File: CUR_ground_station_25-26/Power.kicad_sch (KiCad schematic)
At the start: 32 parts, among them J1 Conn_01x02, J2 UJ20-C-H-G-SMT-P16-TR, Q2 NTR4003N, SW5 PTS815SJM250SMTRLFS, U2 BQ24232RGT, U3 NCP186AMX330TAG, U4 USBLC6-2SC6

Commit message: switched battery connector, put mounting holes in place
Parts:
- J1: footprint Connector_JST:JST_PH_B2B-PH-K_1x02_P2.00mm_Vertical -> Connector_JST:JST_PH_S2B-PH-K_1x02_P2.00mm_Horizontal
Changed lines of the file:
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@@
 			)
 		)
-		(property "Footprint" "Connector_JST:JST_PH_B2B-PH-K_1x02_P2.00mm_Vertical"
+		(property "Footprint" "Connector_JST:JST_PH_S2B-PH-K_1x02_P2.00mm_Horizontal"
 			(at 30.48 30.48 0)
 			(effects

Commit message: labing, adding gnd vias, other cleanup
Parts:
- J1: footprint Connector_JST:JST_PH_S2B-PH-K_1x02_P2.00mm_Horizontal -> Connector_Molex:Molex_PicoBlade_53048-0210_1x02_P1.25mm_Horizontal
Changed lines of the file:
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@@
 			)
 		)
-		(property "Footprint" "Connector_JST:JST_PH_S2B-PH-K_1x02_P2.00mm_Horizontal"
+		(property "Footprint" "Connector_Molex:Molex_PicoBlade_53048-0210_1x02_P1.25mm_Horizontal"
 			(at 30.48 30.48 0)
 			(effects

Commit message: Update gerbers after rotating battery connector
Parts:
- J1: value Conn_01x02 -> 0530480210; MPN (none) -> 0530480210
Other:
- note added: "battery in question"
- note removed: "TODO: choose battery so we know connector and polarity"
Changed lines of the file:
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@@
 		)
 	)
-	(text "TODO:\nchoose battery\nso we know connector\nand polarity"
-		(exclude_from_sim no)
-		(at 40.386 28.448 0)
-		(effects
-			(font
-				(size 1.27 1.27)
-			)
-			(justify left top)
-		)
-	)
 	(text "Battery"
 		(exclude_from_sim no)
@@
 		)
 	)
+	(text "battery in question"
+		(exclude_from_sim no)
+		(at 23.622 48.514 0)
+		(effects
+			(font
+				(size 1.27 1.27)
+			)
+			(href "https://www.amazon.com/MakerHawk-Rechargeable-Protection-Insulated-Development/dp/B0D3LP6F8G")
+		)
+	)
 	(junction
 		(at 144.78 60.96)
@@
 			)
 		)
-		(property "Value" "Conn_01x02"
+		(property "Value" "0530480210"
 			(at 30.48 26.67 0)
 			(effects
@@
 			)
 		)
-		(property "Datasheet" "~"
+		(property "Datasheet" "https://www.molex.com/pdm_docs/sd/530480210_sd.pdf"
 			(at 30.48 30.48 0)
 			(effects
@@
 			(at 30.48 30.48 0)
 			(effects
+				(font
+					(size 1.27 1.27)
+				)
+				(hide yes)
+			)
+		)
+		(property "MPN" "0530480210"
+			(at 30.48 30.48 0)
+			(effects

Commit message: Update LDO and battery charger footprints
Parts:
- U2: footprint Package_DFN_QFN:VQFN-16-1EP_3x3mm_P0.5mm_EP1.68x1.68mm_ThermalVias -> Package_DFN_QFN:VQFN-16-1EP_3x3mm_P0.5mm_EP1.68x1.68mm
- U3: footprint XDFN8_1P6X1P2_onsemi:XDFN8_1P6X1P2_onsemi -> Regulator_Linear_onsemi:NCP186_XDFN8_1.6x1.2mm_P0.4mm
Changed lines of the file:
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@@
 			)
 		)
-		(property "Footprint" "Package_DFN_QFN:VQFN-16-1EP_3x3mm_P0.5mm_EP1.68x1.68mm_ThermalVias"
+		(property "Footprint" "Package_DFN_QFN:VQFN-16-1EP_3x3mm_P0.5mm_EP1.68x1.68mm"
 			(at 129.54 100.965 0)
 			(effects
@@
 			)
 		)
-		(property "Footprint" "XDFN8_1P6X1P2_onsemi:XDFN8_1P6X1P2_onsemi"
+		(property "Footprint" "Regulator_Linear_onsemi:NCP186_XDFN8_1.6x1.2mm_P0.4mm"
 			(at 68.58 114.3 0)
 			(effects

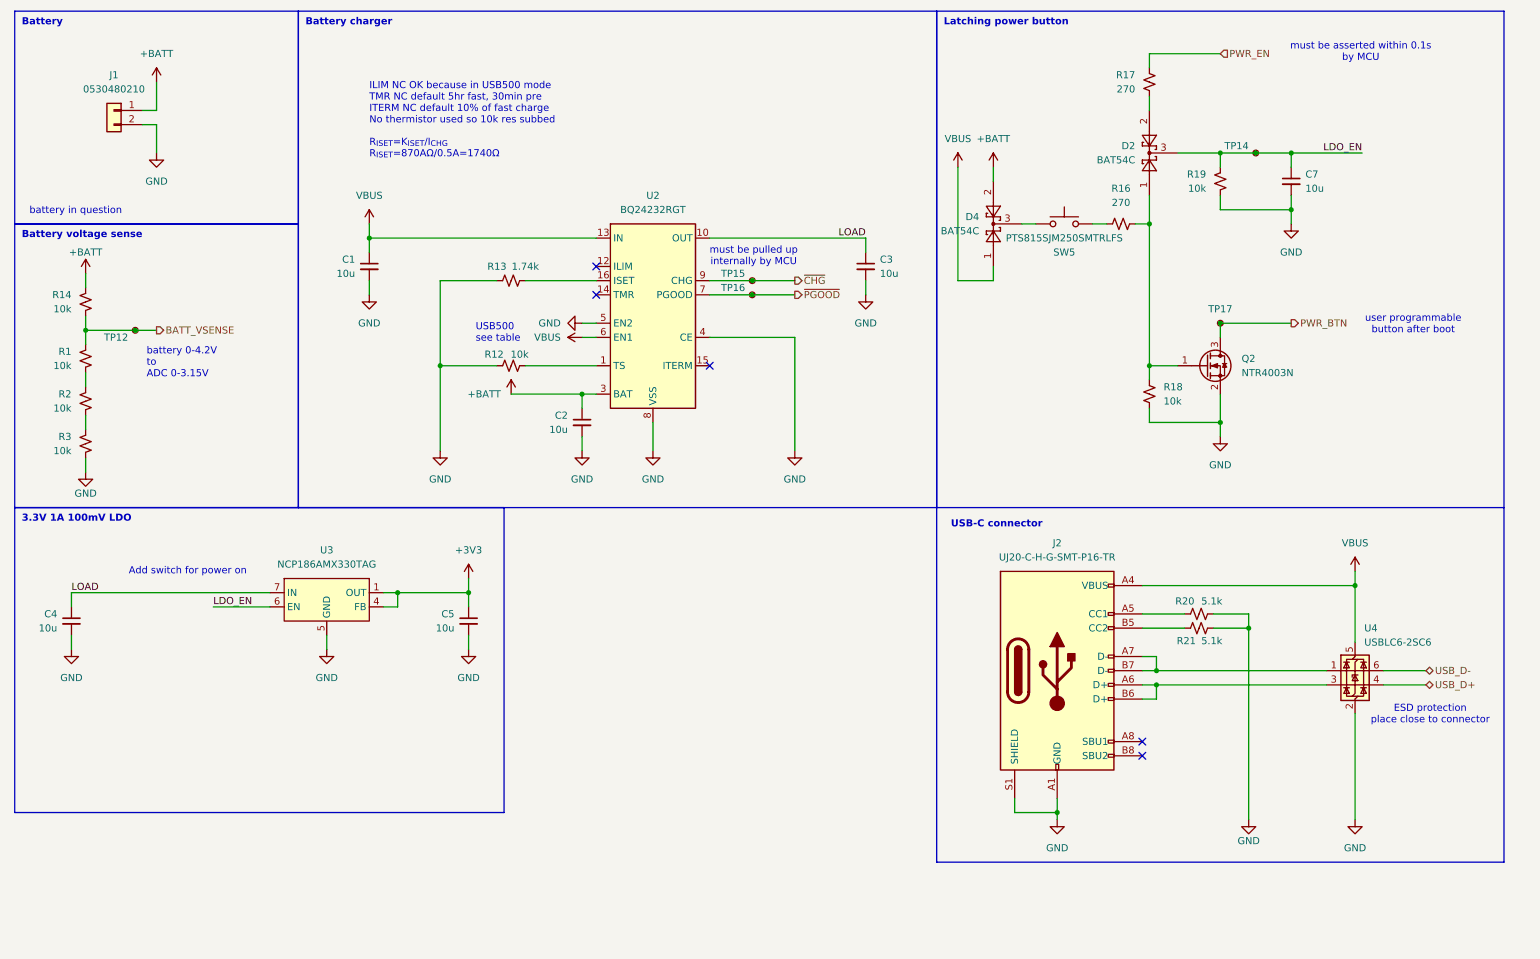
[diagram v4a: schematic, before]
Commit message: Find MPNs again
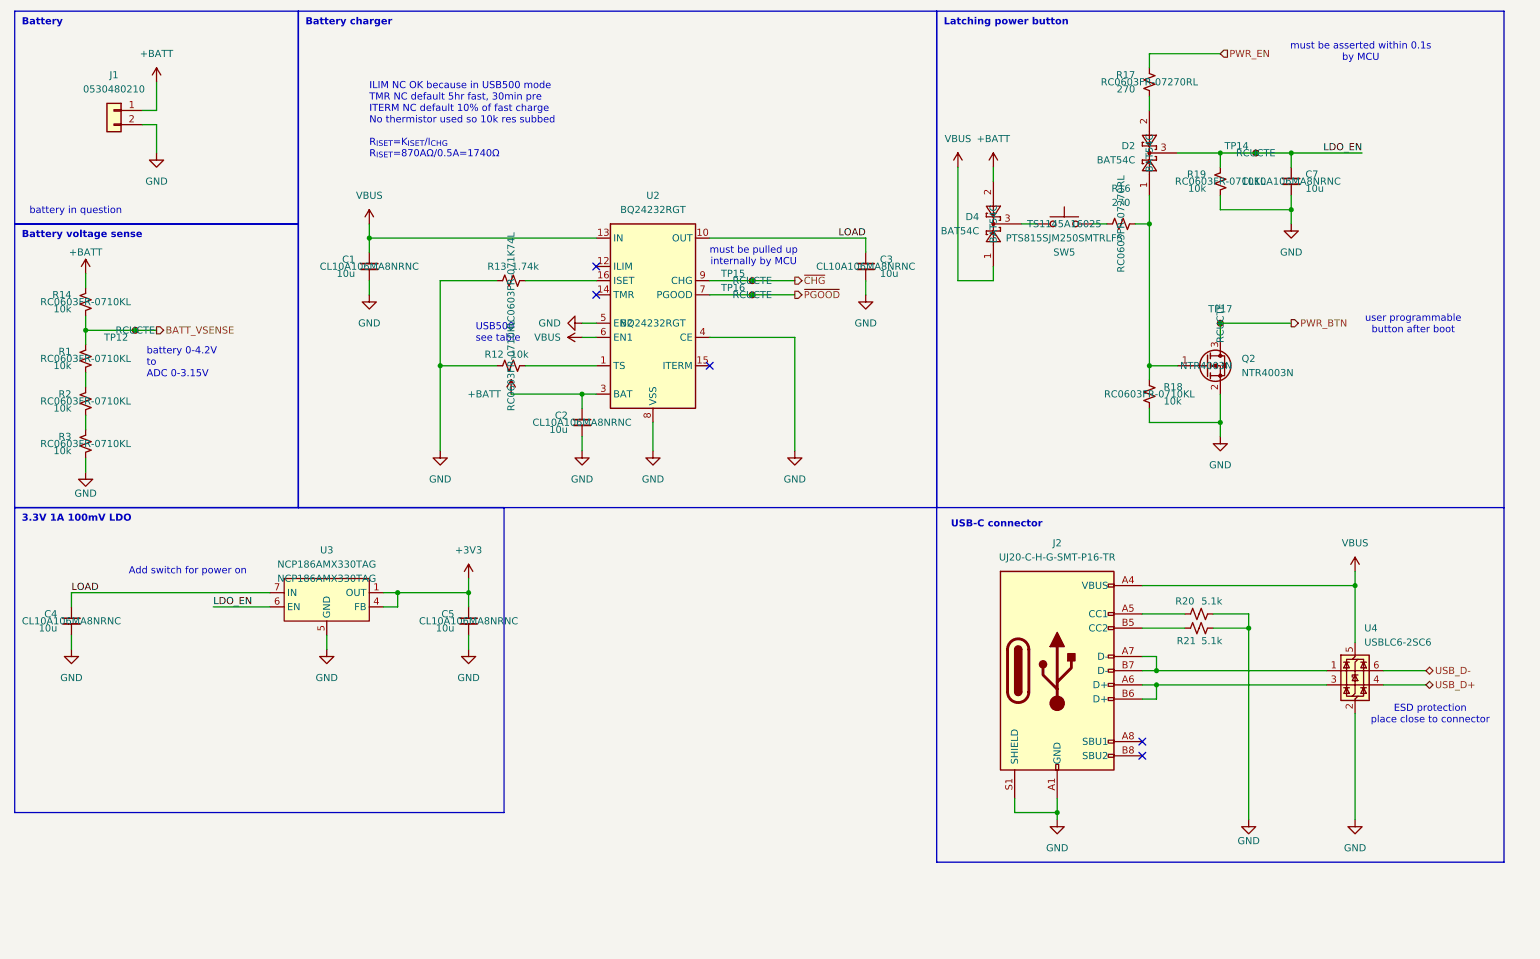
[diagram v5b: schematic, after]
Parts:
- C1, C2, C3, C4, C5, C7: MPN (none) -> CL10A106MA8NRNC
- D2, D4: MPN (none) -> BAT54C
- J1: MPN 0530480210 -> 1.25-2AW
- Q2: MPN (none) -> NTR4003N; now left out of the parts list
- R1, R12, R14, R18, R19, R2, R3: MPN (none) -> RC0603FR-0710KL
- R13: MPN (none) -> RC0603FR-071K74L
- R16, R17: MPN (none) -> RC0603FR-07270RL
- R20, R21: MPN RC0603FR-075K1L -> RC0603FR-075K1L
- SW5: MPN (none) -> TS1145A16025
- TP12, TP14, TP15, TP16, TP17: MPN (none) -> RCUCTE
- U2: MPN (none) -> BQ24232RGT
- U3: MPN (none) -> NCP186AMX330TAG
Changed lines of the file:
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@@
 			)
 		)
+		(property "MPN" "RCUCTE"
+			(at 144.78 60.96 0)
+			(effects
+				(font
+					(size 1.27 1.27)
+				)
+			)
+		)
 		(pin "1"
 		)
@@
 			)
 		)
+		(property "MPN" "CL10A106MA8NRNC"
+			(at 93.98 121.92 0)
+			(effects
+				(font
+					(size 1.27 1.27)
+				)
+			)
+		)
 		(pin "1"
 		)
@@
 			)
 		)
+		(property "MPN" "CL10A106MA8NRNC"
+			(at 241.3 43.18 0)
+			(effects
+				(font
+					(size 1.27 1.27)
+				)
+			)
+		)
 		(pin "2"
 		)
@@
 			)
 		)
+		(property "MPN" "BQ24232RGT"
+			(at 127 68.58 0)
+			(effects
+				(font
+					(size 1.27 1.27)
+				)
+			)
+		)
 		(pin "17"
 		)
@@
 			)
 		)
+		(property "MPN" "NCP186AMX330TAG"
+			(at 68.58 114.3 0)
+			(effects
+				(font
+					(size 1.27 1.27)
+				)
+			)
+		)
 		(pin "7"
 		)
@@
 			)
 		)
+		(property "MPN" "BAT54C"
+			(at 215.9 38.1 0)
+			(effects
+				(font
+					(size 1.27 1.27)
+				)
+			)
+		)
 		(pin "3"
 		)
@@
 			)
 		)
+		(property "MPN" "RC0603FR-0710KL"
+			(at 101.6 76.2 0)
+			(effects
+				(font
+					(size 1.27 1.27)
+				)
+			)
+		)
 		(pin "1"
 		)
@@
 			)
 		)
+		(property "MPN" "RC0603FR-0710KL"
+			(at 25.4 64.77 0)
+			(effects
+				(font
+					(size 1.27 1.27)
+				)
+			)
+		)
 		(pin "2"
 		)
@@
 			)
 		)
+		(property "MPN" "RCUCTE"
+			(at 34.29 69.85 0)
+			(effects
+				(font
+					(size 1.27 1.27)
+				)
+			)
+		)
 		(pin "1"
 		)
@@
 			)
 		)
+		(property "MPN" "RC0603FR-0710KL"
+			(at 25.4 82.55 0)
+			(effects
+				(font
+					(size 1.27 1.27)
+				)
+			)
+		)
 		(pin "2"
 		)
@@
 			)
 		)
-		(property "MPN" "RC0603FR-075K1L"
+		(property "MPN" " RC0603FR-075K1L"
 			(at 224.79 120.65 90)
 			(effects
@@
 			)
 		)
+		(property "MPN" "CL10A106MA8NRNC"
+			(at 165.1 58.42 0)
+			(effects
+				(font
+					(size 1.27 1.27)
+				)
+			)
+		)
 		(pin "2"
 		)
@@
 			)
 		)
+		(property "MPN" "RCUCTE"
+			(at 144.78 63.5 0)
+			(effects
+				(font
+					(size 1.27 1.27)
+				)
+			)
+		)
 		(pin "1"
 		)
@@
 			)
 		)
+		(property "MPN" "RCUCTE"
+			(at 234.95 38.1 0)
+			(effects
+				(font
+					(size 1.27 1.27)
+				)
+			)
+		)
 		(pin "1"
 		)
@@
 			)
 		)
+		(property "MPN" "RC0603FR-0710KL"
+			(at 228.6 43.18 0)
+			(effects
+				(font
+					(size 1.27 1.27)
+				)
+			)
+		)
 		(pin "2"
 		)
@@
 			)
 		)
+		(property "MPN" "CL10A106MA8NRNC"
+			(at 76.2 58.42 0)
+			(effects
+				(font
+					(size 1.27 1.27)
+				)
+			)
+		)
 		(pin "2"
 		)
@@
 			)
 		)
+		(property "MPN" "RC0603FR-071K74L"
+			(at 101.6 60.96 0)
+			(effects
+				(font
+					(size 1.27 1.27)
+				)
+			)
+		)
 		(pin "1"
 		)
@@
 			)
 		)
+		(property "MPN" "RC0603FR-0710KL"
+			(at 25.4 74.93 0)
+			(effects
+				(font
+					(size 1.27 1.27)
+				)
+			)
+		)
 		(pin "2"
 		)
@@
 			)
 		)
+		(property "MPN" "BAT54C"
+			(at 187.96 50.8 0)
+			(effects
+				(font
+					(size 1.27 1.27)
+				)
+			)
+		)
 		(pin "3"
 		)
@@
 			)
 		)
+		(property "MPN" "RC0603FR-07270RL"
+			(at 215.9 25.4 0)
+			(effects
+				(font
+					(size 1.27 1.27)
+				)
+			)
+		)
 		(pin "2"
 		)
@@
 			)
 		)
+		(property "MPN" "TS1145A16025"
+			(at 200.66 50.8 0)
+			(effects
+				(font
+					(size 1.27 1.27)
+				)
+			)
+		)
 		(pin "1"
 		)
@@
 			)
 		)
-		(property "MPN" "0530480210"
+		(property "MPN" "1.25-2AW"
 			(at 30.48 30.48 0)
 			(effects
@@
 			)
 		)
+		(property "MPN" "CL10A106MA8NRNC"
+			(at 22.86 121.92 0)
+			(effects
+				(font
+					(size 1.27 1.27)
+				)
+			)
+		)
 		(pin "1"
 		)
@@
 			)
 		)
-		(property "MPN" "RC0603FR-075K1L"
+		(property "MPN" " RC0603FR-075K1L"
 			(at 224.79 123.19 90)
 			(effects
@@
 			)
 		)
+		(property "MPN" "RCUCTE"
+			(at 228.6 68.58 0)
+			(effects
+				(font
+					(size 1.27 1.27)
+				)
+			)
+		)
 		(pin "1"
 		)
@@
 			)
 		)
+		(property "MPN" "CL10A106MA8NRNC"
+			(at 114.3 86.36 0)
+			(effects
+				(font
+					(size 1.27 1.27)
+				)
+			)
+		)
 		(pin "2"
 		)
@@
 		(unit 1)
 		(exclude_from_sim no)
-		(in_bom yes)
+		(in_bom no)
 		(on_board yes)
 		(dnp no)
@@
 			)
 		)
+		(property "MPN" "NTR4003N"
+			(at 226.06 76.2 0)
+			(effects
+				(font
+					(size 1.27 1.27)
+				)
+			)
+		)
 		(pin "3"
 		)
@@
 			)
 		)
+		(property "MPN" "RC0603FR-0710KL"
+			(at 25.4 90.17 0)
+			(effects
+				(font
+					(size 1.27 1.27)
+				)
+			)
+		)
 		(pin "2"
 		)
@@
 			)
 		)
+		(property "MPN" "RC0603FR-07270RL"
+			(at 210.82 50.8 0)
+			(effects
+				(font
+					(size 1.27 1.27)
+				)
+			)
+		)
 		(pin "1"
 		)
@@
 			)
 		)
+		(property "MPN" "RC0603FR-0710KL"
+			(at 215.9 81.28 0)
+			(effects
+				(font
+					(size 1.27 1.27)
+				)
+			)
+		)

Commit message: changes
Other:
- company: (none) -> Clarkson University Rocketry
- title: (none) -> Ground Station
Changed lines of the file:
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@@
 	(generator_version "9.0")
 	(paper "A4")
+	(title_block
+		(title "Ground Station")
+		(date "2026-04-29")
+		(company "Clarkson University Rocketry")
+	)
 	(rectangle
 		(start 177.8 12.7)
@@
 					(size 1.27 1.27)
 				)
+				(hide yes)
 			)
 		)
@@
 					(size 1.27 1.27)
 				)
+				(hide yes)
 			)
 		)
@@
 					(size 1.27 1.27)
 				)
+				(hide yes)
 			)
 		)
@@
 					(size 1.27 1.27)
 				)
+				(hide yes)
 			)
 		)
@@
 					(size 1.27 1.27)
 				)
+				(hide yes)
 			)
 		)
@@
 					(size 1.27 1.27)
 				)
+				(hide yes)
 			)
 		)
@@
 					(size 1.27 1.27)
 				)
+				(hide yes)
 			)
 		)
@@
 					(size 1.27 1.27)
 				)
+				(hide yes)
 			)
 		)
@@
 					(size 1.27 1.27)
 				)
+				(hide yes)
 			)
 		)
@@
 					(size 1.27 1.27)
 				)
+				(hide yes)
 			)
 		)
@@
 					(size 1.27 1.27)
 				)
+				(hide yes)
 			)
 		)
@@
 					(size 1.27 1.27)
 				)
+				(hide yes)
 			)
 		)
@@
 					(size 1.27 1.27)
 				)
+				(hide yes)
 			)
 		)
@@
 	)
 	(symbol
+		(lib_id "CUR_Logo:LOGO")
+		(at 279.4 173.99 0)
+		(unit 1)
+		(exclude_from_sim no)
+		(in_bom yes)
+		(on_board yes)
+		(dnp no)
+		(fields_autoplaced yes)
+		(property "Reference" "#G4"
+			(at 279.4 167.002 0)
+			(effects
+				(font
+					(size 1.27 1.27)
+				)
+				(hide yes)
+			)
+		)
+		(property "Value" "LOGO"
+			(at 279.4 180.978 0)
+			(effects
+				(font
+					(size 1.27 1.27)
+				)
+				(hide yes)
+			)
+		)
+		(property "Footprint" ""
+			(at 279.4 173.99 0)
+			(effects
+				(font
+					(size 1.27 1.27)
+				)
+				(hide yes)
+			)
+		)
+		(property "Datasheet" ""
+			(at 279.4 173.99 0)
+			(effects
+				(font
+					(size 1.27 1.27)
+				)
+				(hide yes)
+			)
+		)
+		(property "Description" ""
+			(at 279.4 173.99 0)
+			(effects
+				(font
+					(size 1.27 1.27)
+				)
+				(hide yes)
+			)
+		)
+		(instances
+			(project "CUR_ground_station_25-26"
+				(path "/b6f682bd-f29b-4650-adb4-b230be0368ad/81c93bb2-d3b4-4976-ae9e-2e07f946e0a4"
+					(reference "#G4")
+					(unit 1)
+				)
+			)
+		)
+	)
+	(symbol
 		(lib_id "Device:C_Small")
 		(at 76.2 58.42 0)
@@
 					(size 1.27 1.27)
 				)
+				(hide yes)
 			)
 		)
@@
 					(size 1.27 1.27)
 				)
+				(hide yes)
 			)
 		)
@@
 					(size 1.27 1.27)
 				)
+				(hide yes)
 			)
 		)
@@
 					(size 1.27 1.27)
 				)
+				(hide yes)
 			)
 		)
@@
 					(size 1.27 1.27)
 				)
+				(hide yes)
 			)
 		)
@@
 					(size 1.27 1.27)
 				)
+				(hide yes)
 			)
 		)
@@
 					(size 1.27 1.27)
 				)
+				(hide yes)
 			)
 		)
@@
 					(size 1.27 1.27)
 				)
+				(hide yes)
 			)
 		)
@@
 					(size 1.27 1.27)
 				)
+				(hide yes)
 			)
 		)
@@
 					(size 1.27 1.27)
 				)
+				(hide yes)
 			)
 		)
@@
 					(size 1.27 1.27)
 				)
+				(hide yes)
 			)
 		)
@@
 					(size 1.27 1.27)
 				)
+				(hide yes)
 			)
 		)
@@
 					(size 1.27 1.27)
 				)
+				(hide yes)
 			)
 		)
